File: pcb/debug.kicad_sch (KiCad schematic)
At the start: 6 parts, among them J4 TC2030, J5 CNC_Tech_3220-14-0100-00

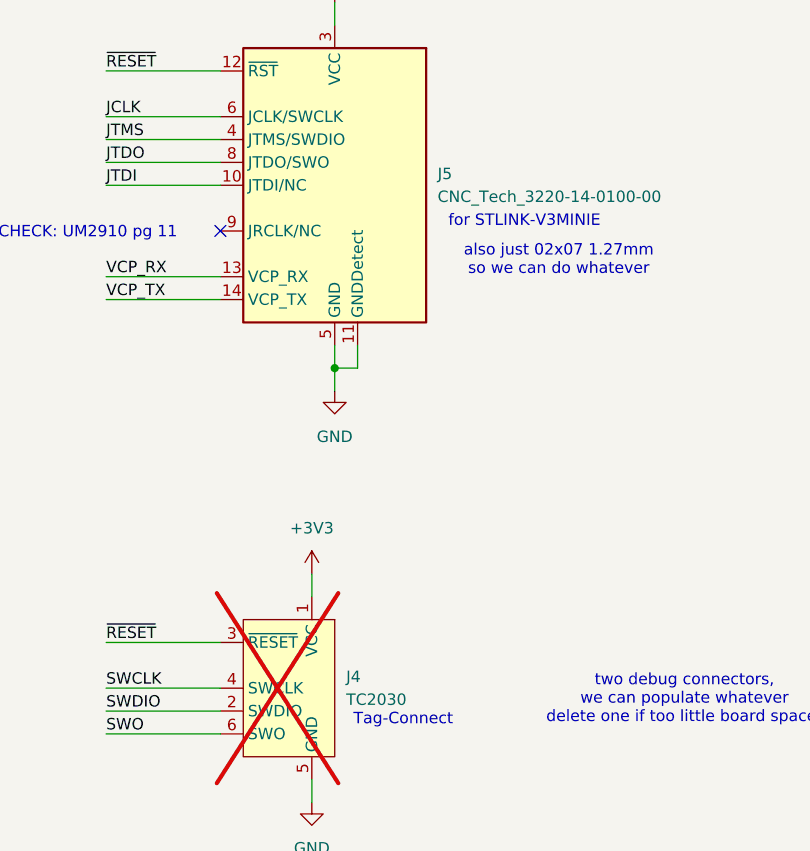
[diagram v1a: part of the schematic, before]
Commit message: Incorporate feedback servo with 4 pin molex and additional ADC channel
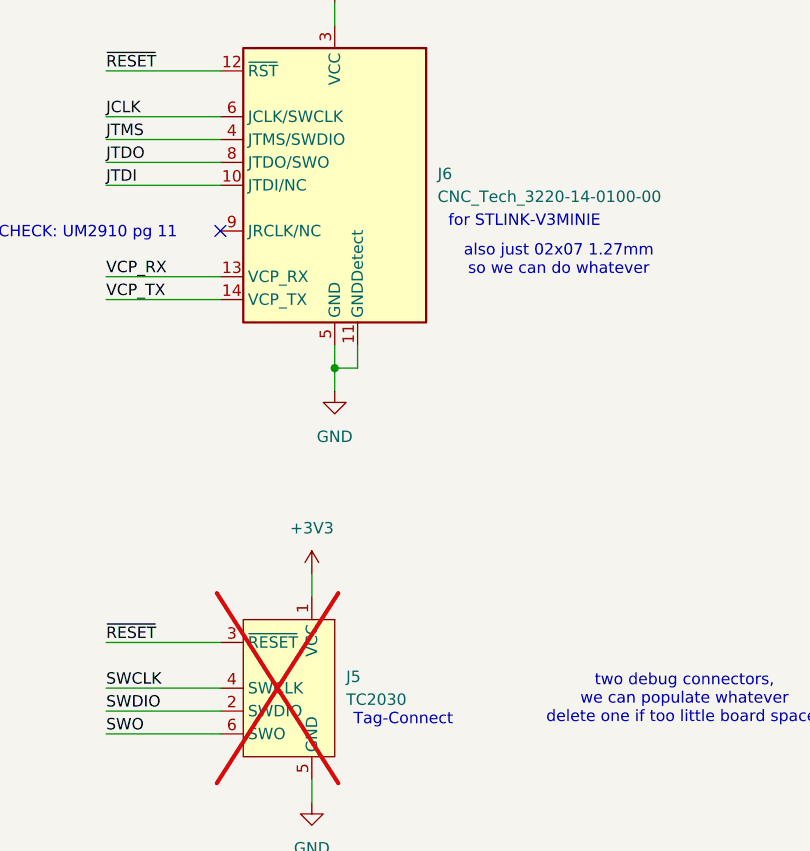
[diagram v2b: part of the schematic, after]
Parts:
- renumbered J4 to J5, J5 to J6
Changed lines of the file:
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@@
 		(dnp no)
 		(fields_autoplaced yes)
-		(property "Reference" "J5"
+		(property "Reference" "J6"
 			(at 151.13 41.9099 0)
 			(effects
@@
 			(project "airbrake_mod"
 				(path "/1f4fd4ed-9886-4375-a5ac-dc32d5760936/3d511e99-5228-4ca9-8dfb-1c1192a39280"
-					(reference "J5")
+					(reference "J6")
 					(unit 1)
 				)
@@
 		(dnp no)
 		(fields_autoplaced yes)
-		(property "Reference" "#PWR071"
+		(property "Reference" "#PWR075"
 			(at 139.7 72.39 0)
 			(effects
@@
 			(project "airbrake_mod"
 				(path "/1f4fd4ed-9886-4375-a5ac-dc32d5760936/3d511e99-5228-4ca9-8dfb-1c1192a39280"
-					(reference "#PWR071")
+					(reference "#PWR075")
 					(unit 1)
 				)
@@
 		(dnp no)
 		(fields_autoplaced yes)
-		(property "Reference" "#PWR068"
+		(property "Reference" "#PWR072"
 			(at 137.16 90.17 0)
 			(effects
@@
 			(project "airbrake_mod"
 				(path "/1f4fd4ed-9886-4375-a5ac-dc32d5760936/3d511e99-5228-4ca9-8dfb-1c1192a39280"
-					(reference "#PWR068")
+					(reference "#PWR072")
 					(unit 1)
 				)
@@
 		(dnp no)
 		(fields_autoplaced yes)
-		(property "Reference" "#PWR069"
+		(property "Reference" "#PWR073"
 			(at 137.16 118.11 0)
 			(effects
@@
 			(project "airbrake_mod"
 				(path "/1f4fd4ed-9886-4375-a5ac-dc32d5760936/3d511e99-5228-4ca9-8dfb-1c1192a39280"
-					(reference "#PWR069")
+					(reference "#PWR073")
 					(unit 1)
 				)
@@
 		(dnp yes)
 		(fields_autoplaced yes)
-		(property "Reference" "J4"
+		(property "Reference" "J5"
 			(at 140.97 97.7899 0)
 			(effects
@@
 			(project ""
 				(path "/1f4fd4ed-9886-4375-a5ac-dc32d5760936/3d511e99-5228-4ca9-8dfb-1c1192a39280"
-					(reference "J4")
+					(reference "J5")
 					(unit 1)
 				)
@@
 		(dnp no)
 		(fields_autoplaced yes)
-		(property "Reference" "#PWR070"
+		(property "Reference" "#PWR074"
 			(at 139.7 26.67 0)
 			(effects
@@
 			(project "airbrake_mod"
 				(path "/1f4fd4ed-9886-4375-a5ac-dc32d5760936/3d511e99-5228-4ca9-8dfb-1c1192a39280"
-					(reference "#PWR070")
-					(unit 1)
-				)
+					(reference "#PWR074")
+					(unit 1)
+				)

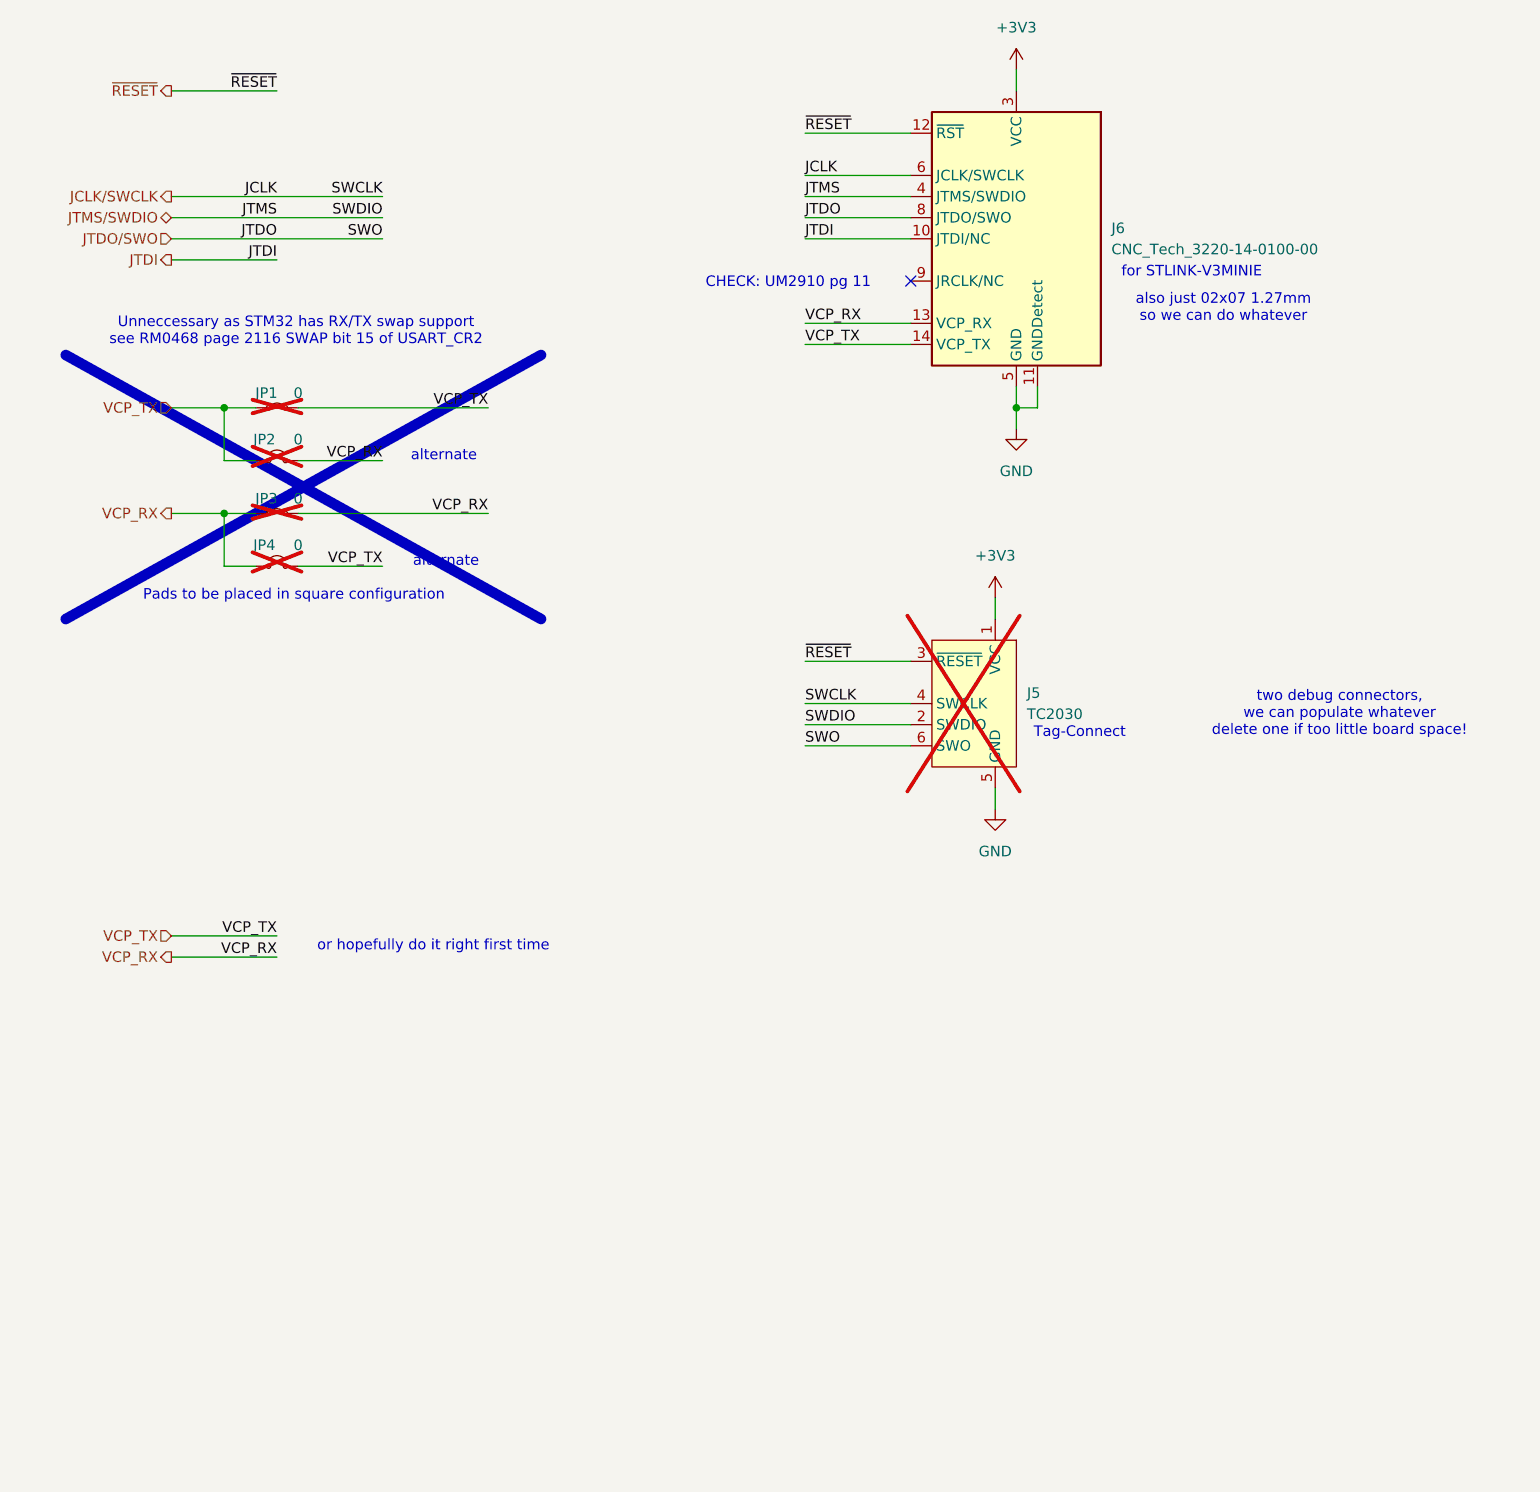
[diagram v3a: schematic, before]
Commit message: Add ESD protection diode arrays
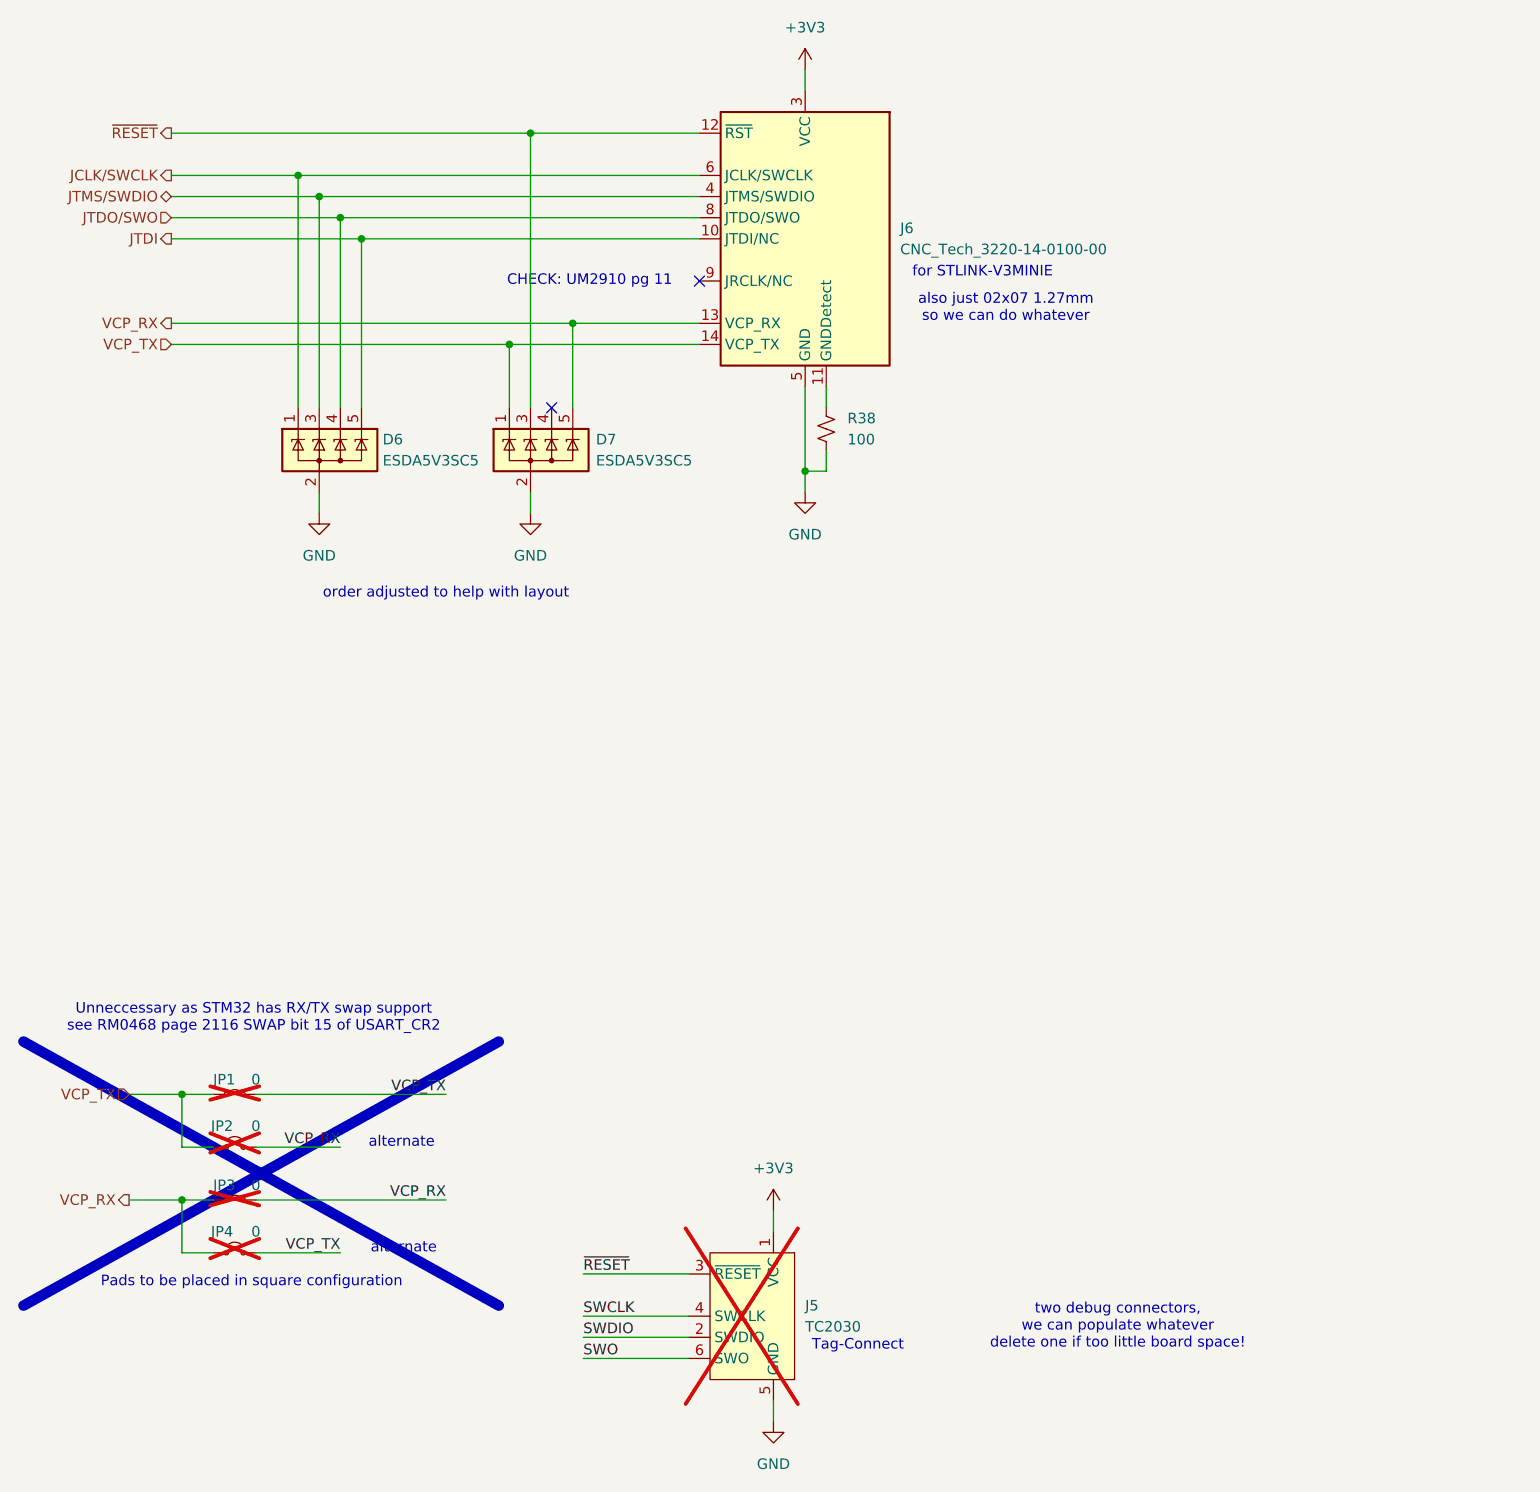
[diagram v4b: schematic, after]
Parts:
- added D6, D7: ESDA5V3SC5, Package_TO_SOT_SMD:SOT-23-5, symbol Power_Protection:ESDA5V3SC5
- added R38: 100, Resistor_SMD:R_0603_1608Metric, symbol Device:R_Small_US
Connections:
- net GND: now also D6.2 (A), D7.2 (A), R38.2; no longer J6.11 (GNDDetect)
- net JCLK/SWCLK: now also D6.1 (K); no longer J5.4 (SWCLK)
- net JTDI: now also D6.5 (K)
- net JTDO/SWO: now also D6.4 (K); no longer J5.6 (SWO)
- net JTMS/SWDIO: now also D6.3 (K); no longer J5.2 (SWDIO)
- net VCP_RX: now also D7.5 (K)
- net VCP_TX: now also D7.1 (K)
- net ~{RESET}: now also D7.3 (K)
- new net: J6.11 (GNDDetect), R38.1
- new net SWCLK: J5.4 (SWCLK)
- new net SWDIO: J5.2 (SWDIO)
- new net SWO: J5.6 (SWO)
- no-connect marks 1 -> 2
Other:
- note added: "order adjusted to help with layout"
- note removed: "or hopefully do it right first time"
- moved on the sheet: J5, J6, JP1, JP2, JP3, JP4

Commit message: Add CUR schematic sheet title block
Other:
- company: (none) -> Clarkson University Rocketry Team
- title: (none) -> Air Brakes Module
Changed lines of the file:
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@@
 	(generator_version "9.0")
 	(paper "A4")
+	(title_block
+		(title "Air Brakes Module")
+		(date "2025-11-23")
+		(company "Clarkson University Rocketry Team")
+	)
 	(text "order adjusted to help with layout"
 		(exclude_from_sim no)
